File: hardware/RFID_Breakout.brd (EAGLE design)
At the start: 25.4 x 25.4 mm, 6 parts, among them U1 RFID

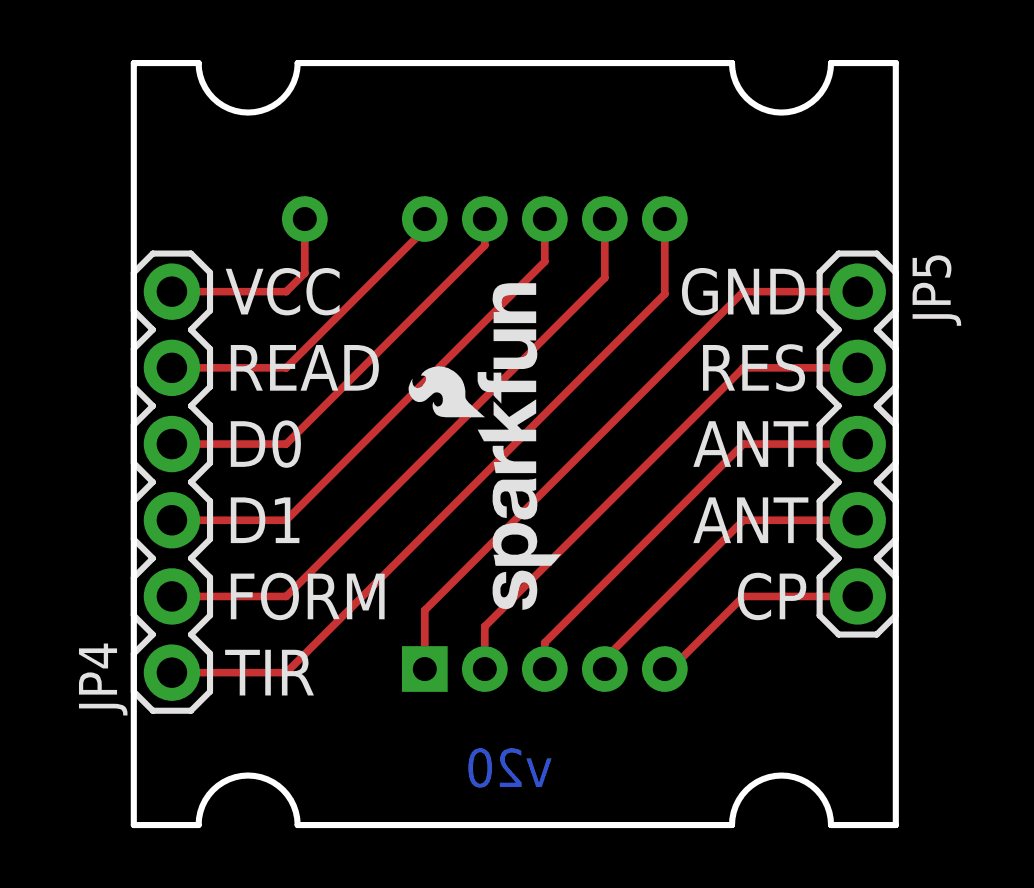
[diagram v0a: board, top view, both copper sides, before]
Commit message: Updating silkscreen to both sides, adding in OSHW logo, adding in bottom copper for version number
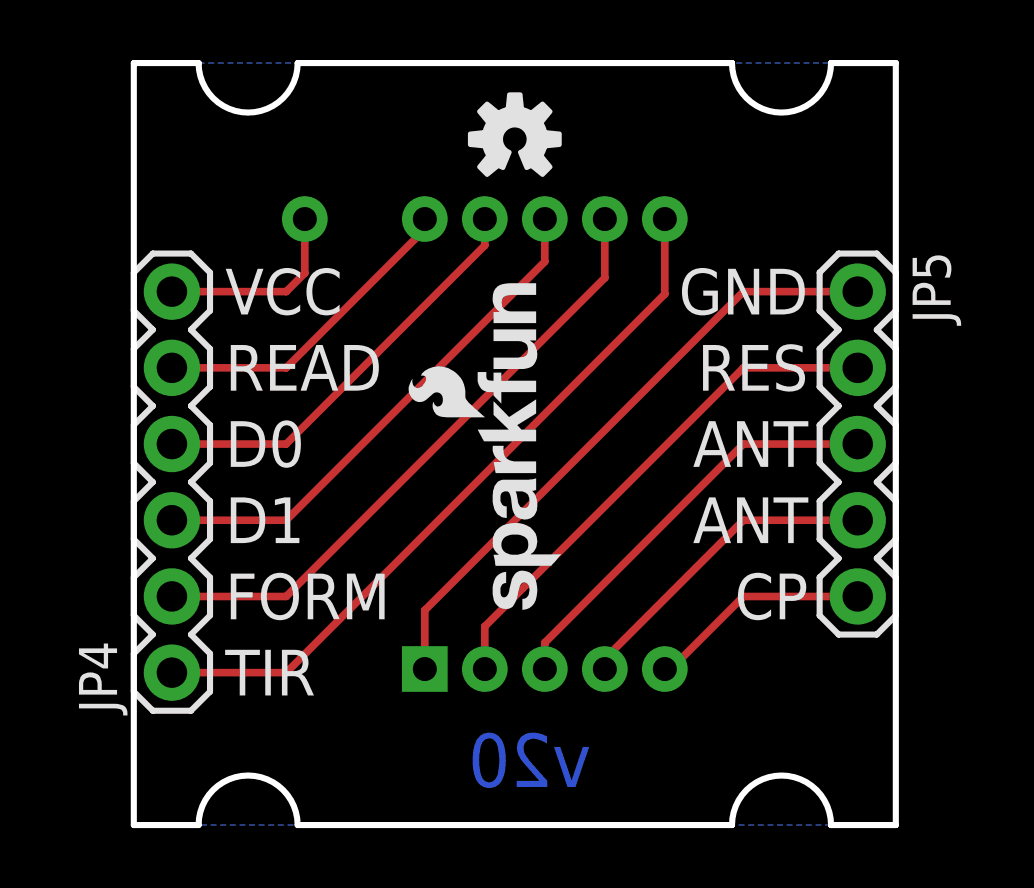
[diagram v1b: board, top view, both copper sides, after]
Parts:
- added LOGO3: OSHW-LOGOS, SparkFun-Aesthetics:OSHW-LOGO-S
- added U$1: REVISION, SparkFun-Aesthetics:REVISION
- LOGO1: value SFE_LOGO_NAME_FLAME.1_INCH -> SFE_LOGO_FLAME.1_INCH; device SparkFun-Aesthetics:SFE_LOGO_NAME_FLAME_.1 -> SparkFun-Aesthetics:SFE_LOGO_FLAME_.1
- moved LOGO1 5.06 mm to (1.27, -3.81)
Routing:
- added copper zone on layer 16, net N$1
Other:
- board text added: "Breakout"
- board text added: "RFID"
- board text added: "Toni Klopfenstein"
- board text removed: "RFID Breakout"
